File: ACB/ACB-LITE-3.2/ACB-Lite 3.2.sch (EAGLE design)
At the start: 238 parts, among them CON2 166087-4, IC1 PIC32MX470F512L-I/PF, IC10 MAX9938HEUK+T, IC11 24LC32A-I/MS, IC12 SN65HVD12D, IC13 REF3025, IC14 TPD2E001DZDR, IC15 TPD2E001DZDR, IC16 MCP6042-I/MS, IC2 L6227Q, IC3 LT3971EMSE, IC6 MIC841LYC, IC7 24LC32A-I/MS, IC9 AT25SF321-SSHD, J1 3-641215-2, J12 USB_A_180, J13 3-641215-2, J14 3-641215-5, J15 3-641215-5, J17 DNP-open-hole, J2 3-641215-2, J3 RJ8-8-180, J4 RJ8-8-180, J5 3-641215-2, J6 3-641215-2, J7 3-641215-2, Q1 SSM6P49NU,LFPZ, Q2 SSM6P49NU,LFPZ, Q3 FDC6330L, Q4 FDG6303N, Q5 FDC6506P, Q6 FDG6303N, Q7 FDC6506P, T1 PIC-OUT, T13 PIC-RPX, T14 PIC-RPX, T15 PIC-OUT, T27 PIC-OUT, T3 PIC-RPX, T32 PIC-OUT, T33 PIC-OUT, T36 PIC-OUT, T37 PIN-AN, T38 PIN-AN, T39 PIN-AN, T40 PIC-RPX, T41 PIC-RPX, T42 PIC-OUT, T43 PIC-RPX, T44 PIC-OUT, T45 PIC-RPX, T5 PIC-OUT, T7 PIC-OUT, X1 8MHz-5x3.2mm

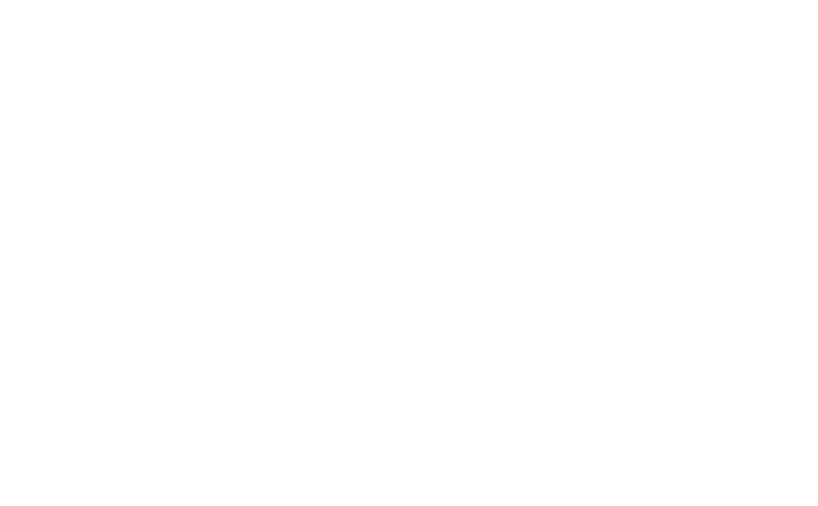
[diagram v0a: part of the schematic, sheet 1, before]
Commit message: adeded ACB LITE 3.2 with fab files
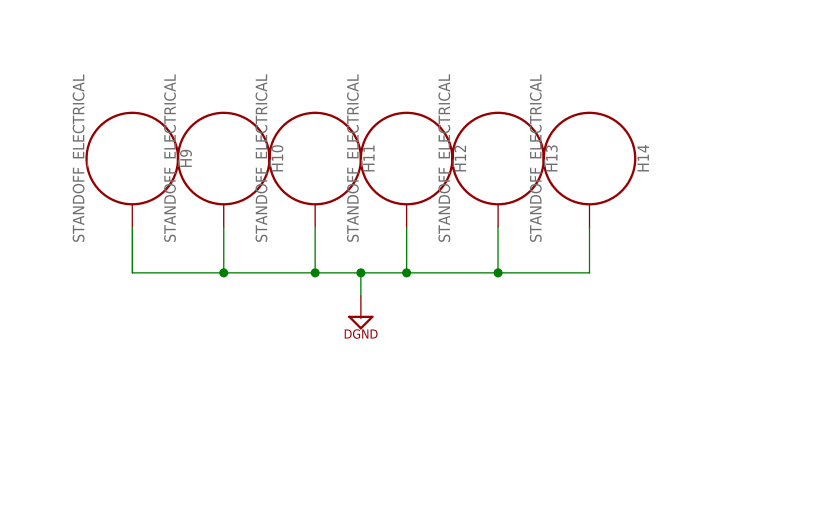
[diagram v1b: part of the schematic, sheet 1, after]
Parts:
- added H10, H11, H12, H13, H14, H9: STANDOFF_ELECTRICAL, SparkFun-Hardware:STANDOFF_ELECTRICAL
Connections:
- net DGND: now also H10.P$1, H11.P$1, H12.P$1, H13.P$1, H14.P$1, H9.P$1
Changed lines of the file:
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@@
 <part name="U$34" library="SUPPLY" deviceset="DGND" device=""/>
 <part name="U$35" library="SUPPLY" deviceset="DGND" device=""/>
+<part name="H9" library="SparkFun-Hardware" deviceset="STANDOFF_ELECTRICAL" device=""/>
+<part name="H10" library="SparkFun-Hardware" deviceset="STANDOFF_ELECTRICAL" device=""/>
+<part name="H11" library="SparkFun-Hardware" deviceset="STANDOFF_ELECTRICAL" device=""/>
+<part name="H12" library="SparkFun-Hardware" deviceset="STANDOFF_ELECTRICAL" device=""/>
+<part name="H13" library="SparkFun-Hardware" deviceset="STANDOFF_ELECTRICAL" device=""/>
+<part name="H14" library="SparkFun-Hardware" deviceset="STANDOFF_ELECTRICAL" device=""/>
+<part name="U$43" library="SUPPLY" deviceset="DGND" device=""/>
 </parts>
 <sheets>
@@
 </instance>
 <instance part="CON2" gate="G$1" x="309.88" y="121.92"/>
+<instance part="H9" gate="G$1" x="20.32" y="259.08" rot="R270"/>
+<instance part="H10" gate="G$1" x="30.48" y="259.08" rot="R270"/>
+<instance part="H11" gate="G$1" x="40.64" y="259.08" rot="R270"/>
+<instance part="H12" gate="G$1" x="50.8" y="259.08" rot="R270"/>
+<instance part="H13" gate="G$1" x="60.96" y="259.08" rot="R270"/>
+<instance part="H14" gate="G$1" x="71.12" y="259.08" rot="R270"/>
+<instance part="U$43" gate="G$1" x="45.72" y="241.3" smashed="yes"/>
 </instances>
 <busses>
@@
 <junction x="297.18" y="116.84"/>
 </segment>
+<segment>
+<pinref part="H9" gate="G$1" pin="P$1"/>
+<wire x1="20.32" y1="251.46" x2="20.32" y2="246.38" width="0.1524" layer="91"/>
+<wire x1="20.32" y1="246.38" x2="30.48" y2="246.38" width="0.1524" layer="91"/>
+<pinref part="H14" gate="G$1" pin="P$1"/>
+<wire x1="30.48" y1="246.38" x2="40.64" y2="246.38" width="0.1524" layer="91"/>
+<wire x1="40.64" y1="246.38" x2="45.72" y2="246.38" width="0.1524" layer="91"/>
+<wire x1="45.72" y1="246.38" x2="50.8" y2="246.38" width="0.1524" layer="91"/>
+<wire x1="50.8" y1="246.38" x2="60.96" y2="246.38" width="0.1524" layer="91"/>
+<wire x1="60.96" y1="246.38" x2="71.12" y2="246.38" width="0.1524" layer="91"/>
+<wire x1="71.12" y1="246.38" x2="71.12" y2="251.46" width="0.1524" layer="91"/>
+<pinref part="H13" gate="G$1" pin="P$1"/>
+<wire x1="60.96" y1="251.46" x2="60.96" y2="246.38" width="0.1524" layer="91"/>
+<junction x="60.96" y="246.38"/>
+<pinref part="H12" gate="G$1" pin="P$1"/>
+<wire x1="50.8" y1="251.46" x2="50.8" y2="246.38" width="0.1524" layer="91"/>
+<junction x="50.8" y="246.38"/>
+<pinref part="H11" gate="G$1" pin="P$1"/>
+<wire x1="40.64" y1="251.46" x2="40.64" y2="246.38" width="0.1524" layer="91"/>
+<junction x="40.64" y="246.38"/>
+<pinref part="H10" gate="G$1" pin="P$1"/>
+<wire x1="30.48" y1="251.46" x2="30.48" y2="246.38" width="0.1524" layer="91"/>
+<junction x="30.48" y="246.38"/>
+<wire x1="45.72" y1="246.38" x2="45.72" y2="243.84" width="0.1524" layer="91"/>
+<junction x="45.72" y="246.38"/>
+<pinref part="U$43" gate="G$1" pin="DGND"/>
+</segment>
 </net>
